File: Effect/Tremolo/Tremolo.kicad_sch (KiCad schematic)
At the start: 30 parts, among them J1 Conn_01x04_Pin, J2 Conn_01x03_Pin, Q1 MBT2222ADW1T1, Q2 BC846, Q4 MMBF5103

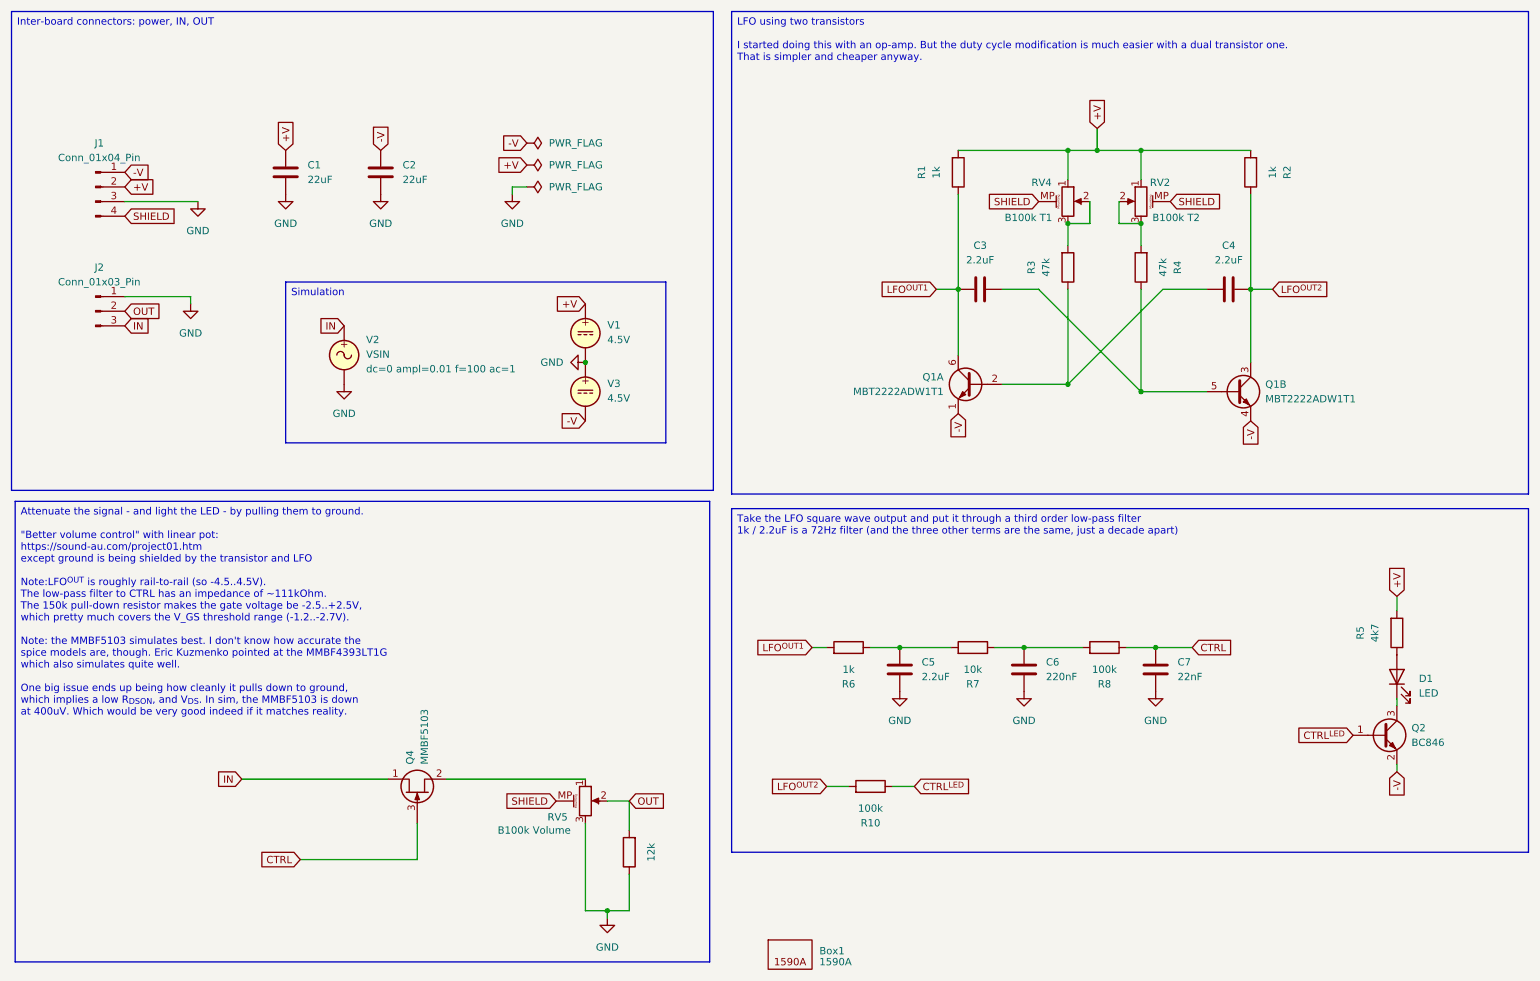
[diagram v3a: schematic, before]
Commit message: Finish up the tremolo pedal. No, really.
This is the end result of the re-org where I use the JFET to switch the
signal rather than as a way to pull it down to ground.  I think I may
have gotten it working now, but hey, I thought that last time too, so
prepare for disappointment.

Signed-off-by: Linus Torvalds <torvalds@linux-foundation.org>
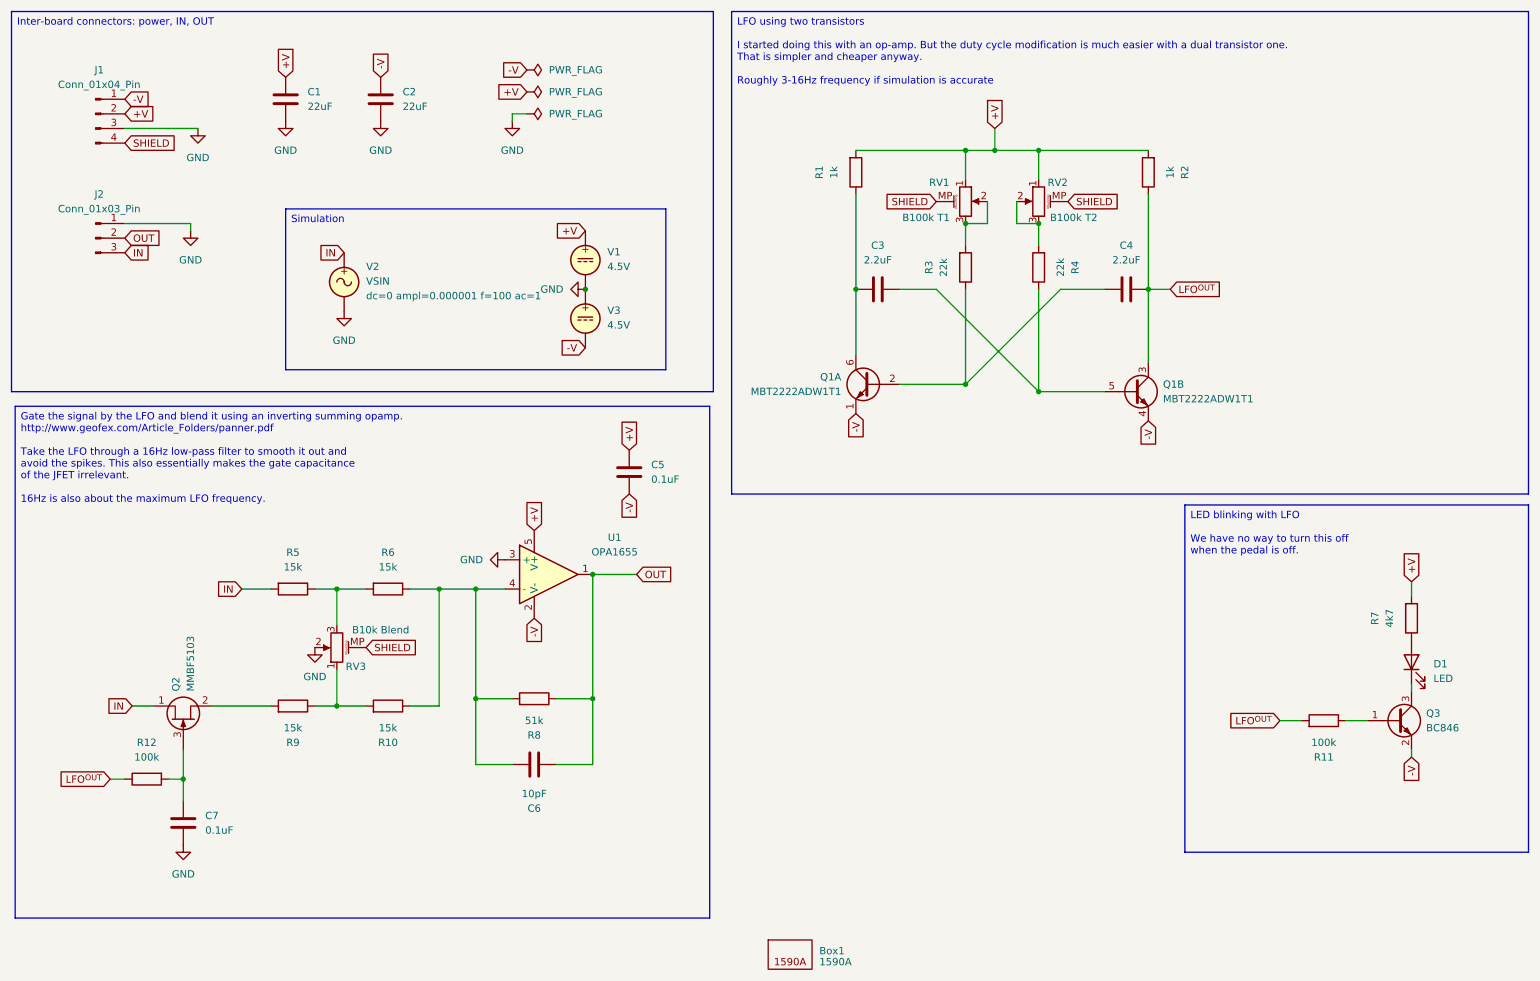
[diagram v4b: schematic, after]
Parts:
- removed R7: 10k, Resistor_SMD:R_0805_2012Metric_Pad1.20x1.40mm_HandSolder, symbol Device:R
- removed RV5: B100k Volume, Mylib:Potentiometer_9mm_MP, symbol Device:R_Potentiometer_MountingPin
- added R10, R5: 15k, Resistor_SMD:R_0805_2012Metric_Pad1.20x1.40mm_HandSolder, symbol Device:R
- added R12: 100k, Resistor_SMD:R_0805_2012Metric_Pad1.20x1.40mm_HandSolder, symbol Device:R
- added RV3: B10k Blend, Mylib:Potentiometer_9mm_MP, symbol Device:R_Potentiometer_MountingPin
- added U1: OPA1655, Package_TO_SOT_SMD:SOT-23-5, symbol Mylib:OPA1655DVB
- C5: value 2.2uF -> 0.1uF; footprint Capacitor_SMD:C_1206_3216Metric_Pad1.33x1.80mm_HandSolder -> Mylib:C_0704_1810Metric
- C6: value 220nF -> 10pF; footprint Capacitor_SMD:C_1206_3216Metric_Pad1.33x1.80mm_HandSolder -> Capacitor_SMD:C_0805_2012Metric_Pad1.18x1.45mm_HandSolder
- C7: value 22nF -> 0.1uF; footprint Capacitor_SMD:C_1206_3216Metric_Pad1.33x1.80mm_HandSolder -> Mylib:C_0704_1810Metric
- R3, R4: value 47k -> 22k
- R6: value 1k -> 15k
- R8: value 100k -> 51k
- R9: value 12k -> 15k
- renumbered Q4 to Q2, Q2 to Q3, R10 to R11, R5 to R7, RV4 to RV1
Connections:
- net +V: now also C5.1, U1.5 (V+)
- net -V: now also C5.2, U1.2 (V-)
- net GND: now also RV3.2, U1.3 (+); no longer C5.1, C6.1, R9.1
- net IN: now also R5.2
- net OUT: now also C6.1, R8.1, U1.1; no longer R9.2
- net SHIELD: now also RV3.MP (MountPin)
- net at C6.2, R8.2: now also R6.1, R10.1, U1.4 (-)
- net at Q2.2 (S): now also R9.2
- net CTRL: no longer names the net of C7.2, Q2.3 (G)
- net CTRL: now also R12.2; no longer R8.1
- net CTRL^{LED}: no longer names the net of Q3.1 (B), R11.1
- net LFO^{OUT1}: no longer names the net of C3.1, Q1.6 (C1), R1.1
- net LFO^{OUT1}: no longer R6.2
- net LFO^{OUT2} renamed LFO^{OUT}
- net LFO^{OUT}: now also R12.1
- new net: R10.2, R9.1, RV3.1
- new net: R5.1, R6.2, RV3.3
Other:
- moved on the sheet: C1, C2, C3, C4, D1, J1, J2, Q1A, Q1B, Q2, Q3, R1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

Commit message: Sometimes I have the mental capacity of a hamster on crack
I'm not making this up - I was looking at the reverse bias leakage of
the JFET, because you can see it show up when the gate voltage goes
sufficiently positive.  And in my infinite wisdom I mentally went "maybe
I should put a diode on the control voltage", and even ended up deciding
to see what that looked like in simulation.

Not my proudest moment.

Only when it made no difference did my reptilian brain go "D'oh".

Let's just change the LFO to oscillate between ground and -V rather than
the whole voltage swing, when we don't actually want to reverse bias
this poor JFET.

And then after that I simulated my old circuit - pre op-amp - and it
worked just fine.  That was a bit odd, becasue I didn't expect this to
really matter, so I went back and forth on the LFO voltage swing, and it
really doesn't matter all that much.

Sure, the negative-only LFO was better, but it wasn't enormously better,
We're talking tens of uV in simulation.  uV, not mV.  And either way the
"make JFET pull to ground" circuit was doing really well.

That was strange too, because the reason I had done the op-amp thing in
the first place was that I couldn't get to those kinds of numbers with
that circuit.

Or so I thought.

I don't know what my problem was.  I'm wondering whether I saw those uV
numbers, and didn't react to the 'u' part, and thought I was still in
the mV range.  Regardless, I've gone back and simulated things again,
and the old simpler JFET circuit simply looks better.

[ For next time this happens: I think I got confused because I simulated
  a 1mV signal and compared that to something a bit saner.

  Simulate no signal at all to see just the switching noise, and a ~0.1V
  amplitude signal for a "somewhat realistic guitar volume", but a 1mV
  signal makes little sense ]

I must have had some hamster-brain moment, but now I can't replicate my
problems from before and I'm not sure what I changed.  I was playing
around tweaki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
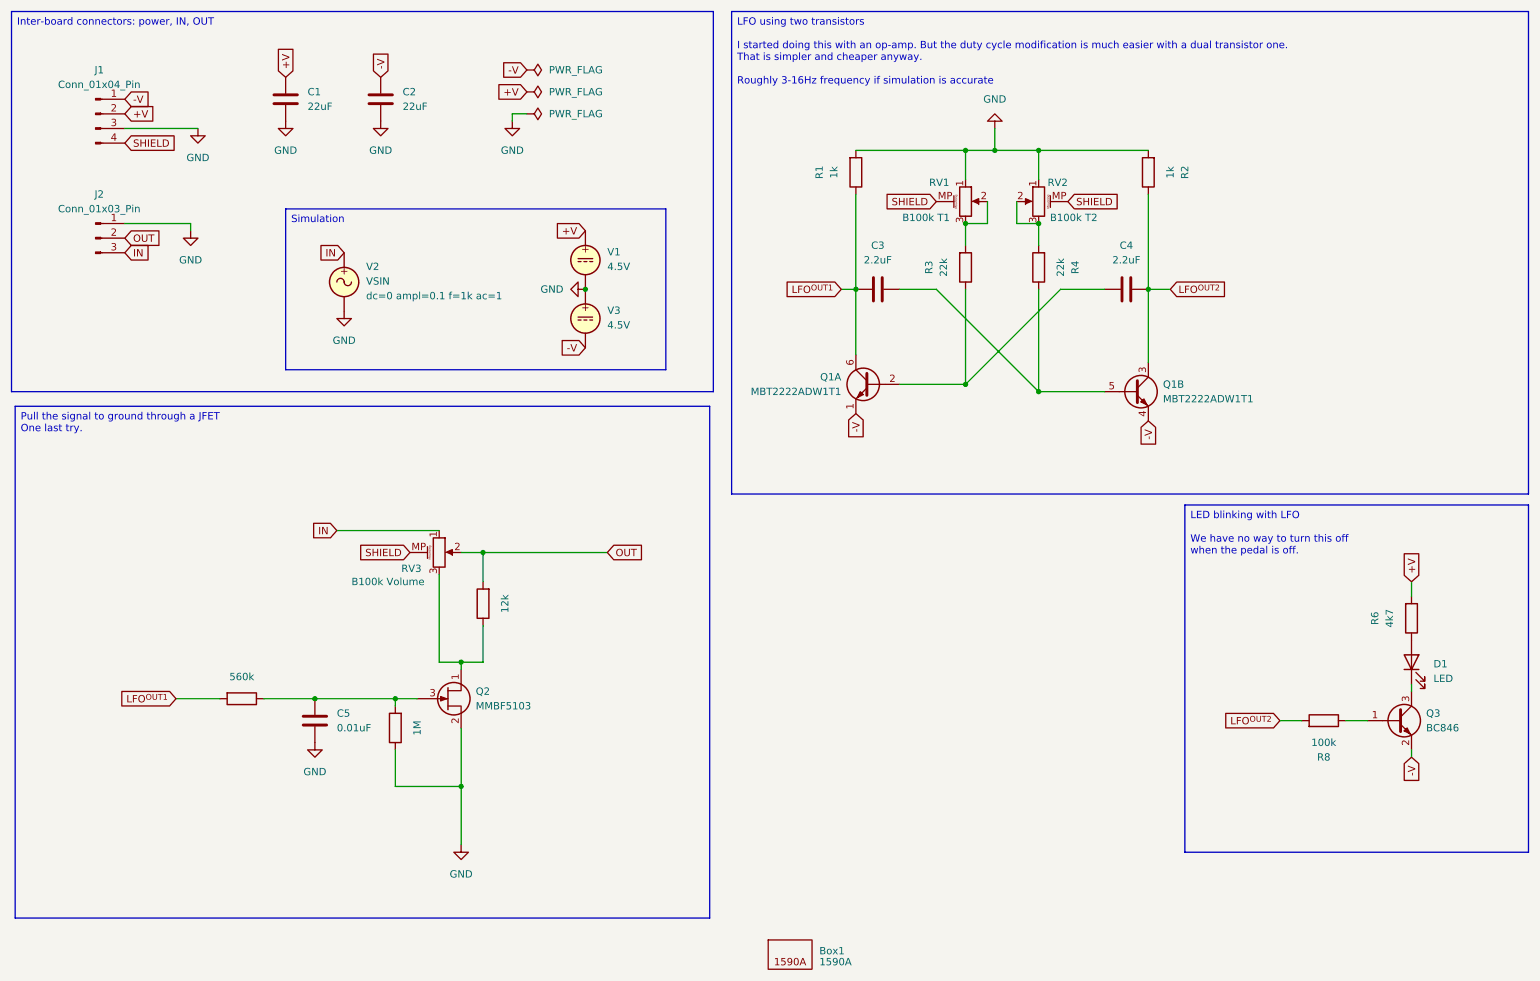
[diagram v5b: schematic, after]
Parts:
- removed C6: 10pF, Capacitor_SMD:C_0805_2012Metric_Pad1.18x1.45mm_HandSolder, symbol Device:C
- removed C7: 0.1uF, Mylib:C_0704_1810Metric, symbol Device:C
- removed R10, R6: 15k, Resistor_SMD:R_0805_2012Metric_Pad1.20x1.40mm_HandSolder, symbol Device:R
- removed R12: 100k, Resistor_SMD:R_0805_2012Metric_Pad1.20x1.40mm_HandSolder, symbol Device:R
- removed R8: 51k, Resistor_SMD:R_0805_2012Metric_Pad1.20x1.40mm_HandSolder, symbol Device:R
- removed U1: OPA1655, Package_TO_SOT_SMD:SOT-23-5, symbol Mylib:OPA1655DVB
- added R7: 560k, Resistor_SMD:R_0805_2012Metric_Pad1.20x1.40mm_HandSolder, symbol Device:R
- C5: value 0.1uF -> 0.01uF; footprint Mylib:C_0704_1810Metric -> Capacitor_SMD:C_0805_2012Metric_Pad1.18x1.45mm_HandSolder
- R5: value 15k -> 12k
- R9: value 15k -> 1M
- RV3: value B10k Blend -> B100k Volume
- renumbered R7 to R6, R11 to R8
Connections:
- net +V: no longer C5.1, R1.2, R2.2, RV1.1, RV2.1
- net -V: no longer C5.2
- net GND: now also C5.1, Q2.2 (S), R1.2, R2.2, R9.1, RV1.1, RV2.1; no longer RV3.2
- net IN: now also RV3.1; no longer Q2.1 (D), R5.2
- net OUT: now also R5.2, RV3.2
- net at Q2.3 (G): now also C5.2, R9.2, R7.1
- net at R5.1, RV3.3: now also Q2.1 (D)
- net LFO^{OUT1}: now reaches C3.1, Q1.6 (C1), R1.1
- net LFO^{OUT1}: now also R7.2
- net LFO^{OUT} renamed LFO^{OUT2}

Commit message: Quick dirty fix for tremolo board
Bah. This didn't show up in simulation, because I'm stupid.

My "clever" trick to make the LFO output stay negative by using GND as
the upper voltage rail was absolutely moronic.  Why? Because in the VGND
model, GND is not really a power rail at all, just a reference voltage.

Sure, it's a pretty strong reference with the TLE2426 being able to put
some effort into it, but not *that* strong.  It's like 20mA max (I'm not
sure where I got the 80mA number that I have in the VGND schematic, but
it's wrong).

Anyway, there's a much better way to do this - tie the top of the LFO up
to the actual positive power rail, but with a 1k resistor.  That creates
a voltage divider with the resistors to the capacitors, and now we're
not stressing that virtual ground.

And the simulation setup doesn't know that GND is current-limited, so it
didn't show up there, and only when I got a test board back did I go
"why is GNDREF wiggling around like mad? Oh..."

This is a very quick hack - I should think about this more, but even if
it is the right solution and it works I should lay the board out anew.
Instead I just did a hacky minimal re-routing for the nets that changed.
Ugly, but I won't bother doin ga better job unless this actually works
and fixes things.

The good news is that apart from the 10kHz GNDREF oscillation the new
Tremolo board seemed to work.  Of course, that noise could be hiding
other problems, and maybe there's something else wrong.  So let's not
celebrate too early.

Signed-off-by: Linus Torvalds <torvalds@linux-foundation.org>
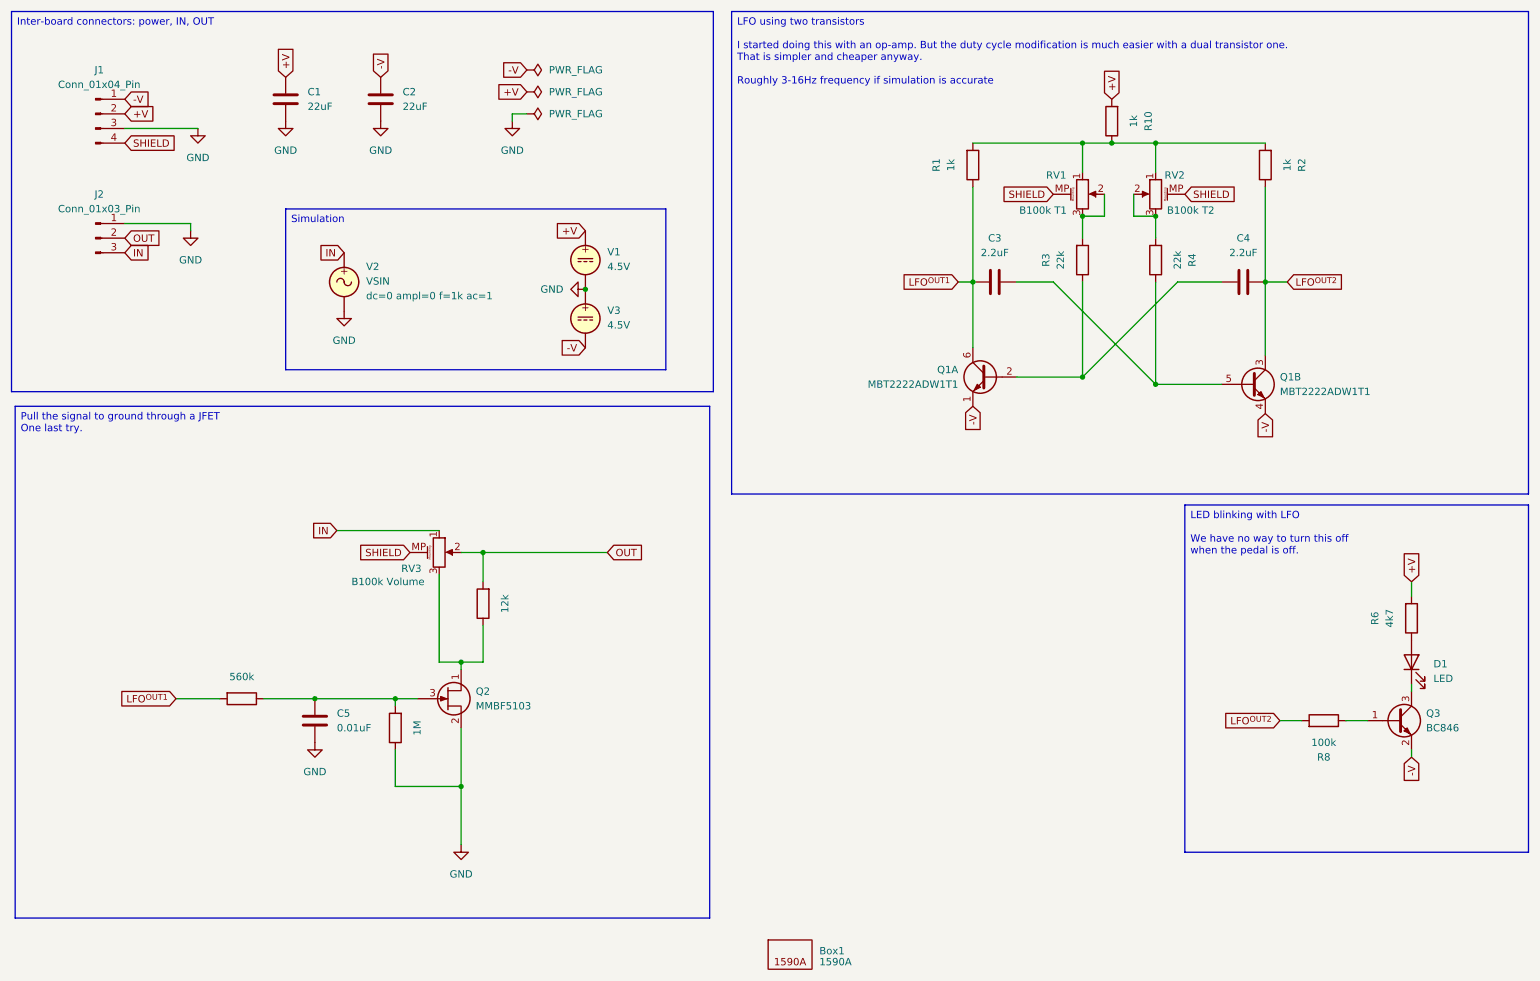
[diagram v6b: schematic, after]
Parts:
- added R10: 1k, Resistor_SMD:R_0805_2012Metric_Pad1.20x1.40mm_HandSolder, symbol Device:R
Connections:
- net +V: now also R10.2
- net GND: no longer R1.2, R2.2, RV1.1, RV2.1
- new net: R1.2, R10.1, R2.2, RV1.1, RV2.1
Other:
- moved on the sheet: C3, C4, Q1A, Q1B, R1, R2, R3, R4, RV1, RV2
